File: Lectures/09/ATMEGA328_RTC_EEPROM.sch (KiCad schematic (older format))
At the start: 33 parts, among them Q1 IRLML6401, SW1 SW_SPST, U1 ATmega328P-AU, U2 24LC1025, U3 24LC1025, U4 DS1337S+, Y1 16MHz, Y2 32.768kHz

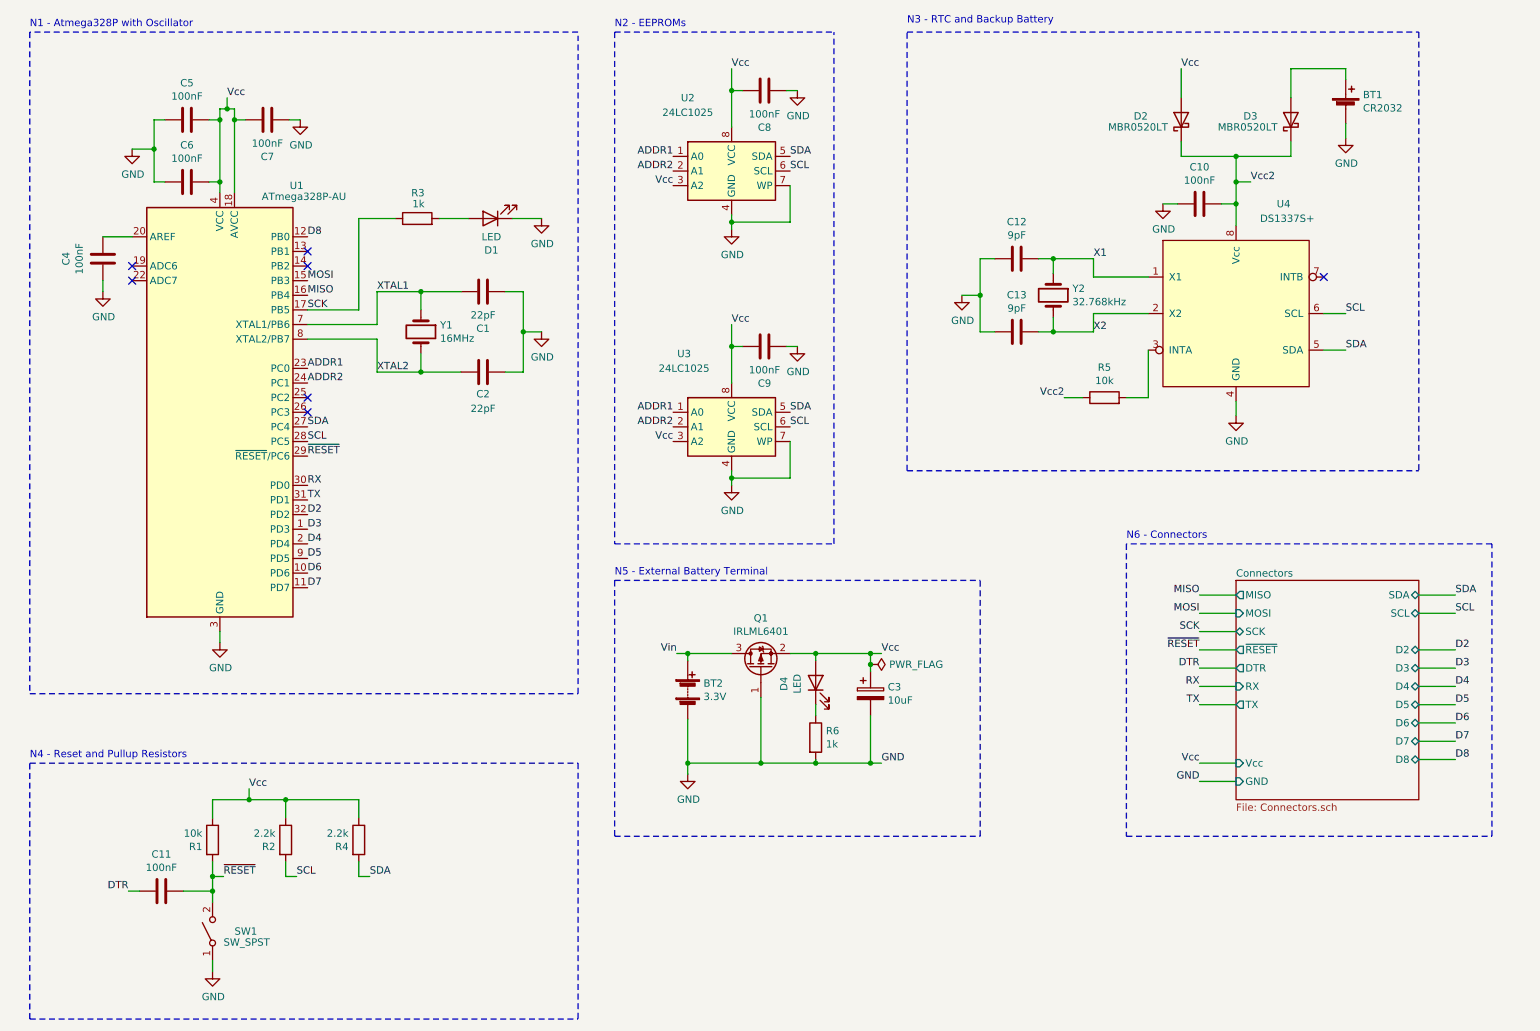
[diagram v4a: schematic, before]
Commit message: ATMEGA328 Layout
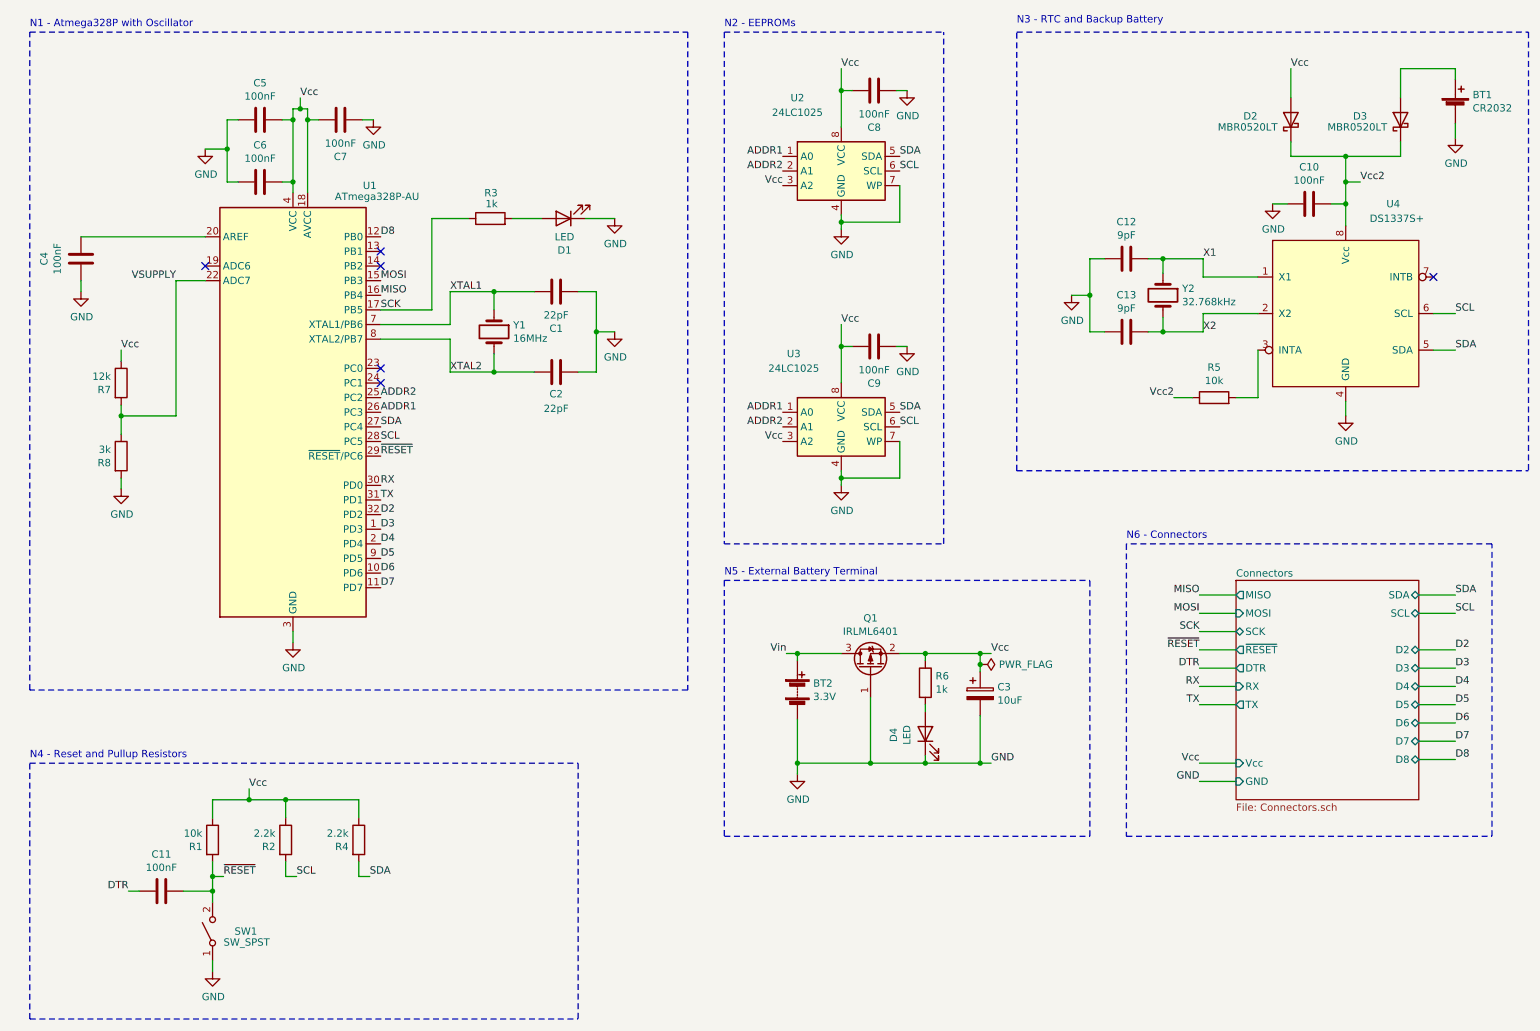
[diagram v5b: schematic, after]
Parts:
- added R7: 12k, Resistor_SMD:R_0805_2012Metric, symbol Device:R
- added R8: 3k, Resistor_SMD:R_0805_2012Metric, symbol Device:R
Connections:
- net ADDR1: now also U1.26 (PC3); no longer U1.23 (PC0)
- net ADDR2: now also U1.25 (PC2); no longer U1.24 (PC1)
- net GND: now also D4.1 (K), R8.2; no longer R6.2
- net Vcc: now also R6.1, R7.1; no longer D4.2 (A)
- net VSUPPLY: now reaches U1.22 (ADC7)
- net VSUPPLY: now also R7.2, R8.1
- new net: D4.2 (A), R6.2
- no-connect marks 7 -> 6
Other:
- moved on the sheet: BT1, BT2, C1, C10, C12, C13, C2, C3, C4, C5, C6, C7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

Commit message: Addressing and Silkscreen
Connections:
- net ADDR1: now also U1.25 (PC2); no longer U1.26 (PC3), U3.1 (A0)
- net ADDR2: now also U1.26 (PC3); no longer U1.25 (PC2), U2.2 (A1)
- net GND: now also U2.2 (A1)
- net Vcc: now also U3.1 (A0)
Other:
- moved on the sheet: C8, C9, U2, U3
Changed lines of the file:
@@
 	7500 3750 11000 3750
 Wire Notes Line
-	7000 4250 7000 750
+	7250 4250 7250 750
 Wire Notes Line
 	5500 750  5500 4250
-Wire Notes Line
-	5500 4250 7000 4250
-Text Label 6300 2750 0    50   ~ 0
+Text Label 6550 2825 0    50   ~ 0
 Vcc
 $Comp
 L Device:C C9
 U 1 1 601B0C2E
-P 6525 2900
-F 0 "C9" V 6273 2900 50  0000 C CNN
-F 1 "100nF" V 6364 2900 50  0000 C CNN
-F 2 "Capacitor_SMD:C_0603_1608Metric" H 6563 2750 50  0001 C CNN
-F 3 "~" H 6525 2900 50  0001 C CNN
-	1    6525 2900
-	0    -1   -1   0
-$EndComp
-Wire Wire Line
-	6300 3150 6300 2900
-Wire Wire Line
-	6300 2900 6375 2900
+P 6775 2900
+F 0 "C9" V 6523 2900 50  0000 C CNN
+F 1 "100nF" V 6614 2900 50  0000 C CNN
+F 2 "Capacitor_SMD:C_0603_1608Metric" H 6813 2750 50  0001 C CNN
+F 3 "~" H 6775 2900 50  0001 C CNN
+	1    6775 2900
+	0    -1   -1   0
+$EndComp
+Wire Wire Line
+	6550 3150 6550 2900
+Wire Wire Line
+	6550 2900 6625 2900
 $Comp
 L power:GND #PWR010
 U 1 1 601B0C26
-P 6750 2900
-F 0 "#PWR010" H 6750 2650 50  0001 C CNN
-F 1 "GND" H 6755 2727 50  0000 C CNN
-F 2 "" H 6750 2900 50  0001 C CNN
-F 3 "" H 6750 2900 50  0001 C CNN
-	1    6750 2900
-	1    0    0    -1
-$EndComp
-Wire Wire Line
-	6750 2900 6675 2900
-Wire Wire Line
-	6300 2900 6300 2750
-Connection ~ 6300 2900
-Text Label 6300 1000 0    50   ~ 0
+P 7000 2900
+F 0 "#PWR010" H 7000 2650 50  0001 C CNN
+F 1 "GND" H 7005 2727 50  0000 C CNN
+F 2 "" H 7000 2900 50  0001 C CNN
+F 3 "" H 7000 2900 50  0001 C CNN
+	1    7000 2900
+	1    0    0    -1
+$EndComp
+Wire Wire Line
+	7000 2900 6925 2900
+Text Label 6550 1075 0    50   ~ 0
 Vcc
 $Comp
 L Device:C C8
 U 1 1 6019A0DD
-P 6525 1150
-F 0 "C8" V 6273 1150 50  0000 C CNN
-F 1 "100nF" V 6364 1150 50  0000 C CNN
-F 2 "Capacitor_SMD:C_0603_1608Metric" H 6563 1000 50  0001 C CNN
-F 3 "~" H 6525 1150 50  0001 C CNN
-	1    6525 1150
-	0    -1   -1   0
-$EndComp
-Wire Wire Line
-	6300 1400 6300 1150
-Wire Wire Line
-	6300 1150 6375 1150
+P 6775 1150
+F 0 "C8" V 6523 1150 50  0000 C CNN
+F 1 "100nF" V 6614 1150 50  0000 C CNN
+F 2 "Capacitor_SMD:C_0603_1608Metric" H 6813 1000 50  0001 C CNN
+F 3 "~" H 6775 1150 50  0001 C CNN
+	1    6775 1150
+	0    -1   -1   0
+$EndComp
+Wire Wire Line
+	6550 1400 6550 1150
+Wire Wire Line
+	6550 1150 6625 1150
 $Comp
 L power:GND #PWR09
 U 1 1 601A1158
-P 6750 1150
-F 0 "#PWR09" H 6750 900 50  0001 C CNN
-F 1 "GND" H 6755 977 50  0000 C CNN
-F 2 "" H 6750 1150 50  0001 C CNN
-F 3 "" H 6750 1150 50  0001 C CNN
-	1    6750 1150
-	1    0    0    -1
-$EndComp
-Wire Wire Line
-	6750 1150 6675 1150
-Wire Wire Line
-	6300 1150 6300 1000
-Connection ~ 6300 1150
+P 7000 1150
+F 0 "#PWR09" H 7000 900 50  0001 C CNN
+F 1 "GND" H 7005 977 50  0000 C CNN
+F 2 "" H 7000 1150 50  0001 C CNN
+F 3 "" H 7000 1150 50  0001 C CNN
+	1    7000 1150
+	1    0    0    -1
+$EndComp
+Wire Wire Line
+	7000 1150 6925 1150
 $Comp
 L power:GND #PWR08
 U 1 1 600E01FF
-P 6300 3850
-F 0 "#PWR08" H 6300 3600 50  0001 C CNN
-F 1 "GND" H 6305 3677 50  0000 C CNN
-F 2 "" H 6300 3850 50  0001 C CNN
-F 3 "" H 6300 3850 50  0001 C CNN
-	1    6300 3850
-	1    0    0    -1
-$EndComp
-$Comp
-L power:GND #PWR07
-U 1 1 600DFD7C
-P 6300 2100
-F 0 "#PWR07" H 6300 1850 50  0001 C CNN
-F 1 "GND" H 6305 1927 50  0000 C CNN
-F 2 "" H 6300 2100 50  0001 C CNN
-F 3 "" H 6300 2100 50  0001 C CNN
-	1    6300 2100
+P 6550 3925
+F 0 "#PWR08" H 6550 3675 50  0001 C CNN
+F 1 "GND" H 6555 3752 50  0000 C CNN
+F 2 "" H 6550 3925 50  0001 C CNN
+F 3 "" H 6550 3925 50  0001 C CNN
+	1    6550 3925
 	1    0    0    -1
 $EndComp
 Text Notes 5500 725  0    50   ~ 0
 N2 - EEPROMs
-Wire Notes Line
-	5500 750  7000 750
-Wire Wire Line
-	6300 2050 6300 2000
-Connection ~ 6300 2050
-Wire Wire Line
-	6700 2050 6300 2050
-Wire Wire Line
-	6700 1800 6700 2050
-Wire Wire Line
-	6300 3800 6300 3750
-Connection ~ 6300 3800
-Wire Wire Line
-	6700 3800 6300 3800
-Wire Wire Line
-	6700 3550 6700 3800
-Wire Wire Line
-	6300 3850 6300 3800
-Text Label 5900 3450 2    50   ~ 0
-ADDR2
-Text Label 5900 1700 2    50   ~ 0
-ADDR2
-Text Label 5900 1600 2    50   ~ 0
-ADDR1
-Text Label 5900 3350 2    50   ~ 0
-ADDR1
-Text Label 6700 3350 0    50   ~ 0
+Text Label 6950 3350 0    50   ~ 0
 SDA
-Text Label 6700 1600 0    50   ~ 0
+Text Label 6950 1600 0    50   ~ 0
 SDA
-Text Label 6700 3450 0    50   ~ 0
+Text Label 6950 3450 0    50   ~ 0
 SCL
-Text Label 6700 1700 0    50   ~ 0
+Text Label 6950 1700 0    50   ~ 0
 SCL
-Text Label 5900 3550 2    50   ~ 0
-Vcc
-Text Label 5900 1800 2    50   ~ 0
-Vcc
-Wire Wire Line
-	6300 2100 6300 2050
-$Comp
-L Memory_EEPROM:24LC1025 U2
-U 1 1 60098B6E
-P 6300 1700
-F 0 "U2" H 6000 2200 50  0000 C CNN
-F 1 "24LC1025" H 6000 2100 50  0000 C CNN
-F 2 "Package_SO:SOIJ-8_5.3x5.3mm_P1.27mm" H 6300 1700 50  0001 C CNN
-F 3 "http://ww1.microchip.com/downloads/en/DeviceDoc/21941B.pdf" H 6300 1700 50  0001 C CNN
-	1    6300 1700
-	1    0    0    -1
-$EndComp
+Text Label 6150 3550 2    50   ~ 0
+Vcc
+Text Label 6150 1800 2    50   ~ 0
+Vcc
 $Comp
 L Memory_EEPROM:24LC1025 U3
 U 1 1 600AAAA0
-P 6300 3450
-F 0 "U3" H 5975 3950 50  0000 C CNN
-F 1 "24LC1025" H 5975 3850 50  0000 C CNN
-F 2 "Package_SO:SOIJ-8_5.3x5.3mm_P1.27mm" H 6300 3450 50  0001 C CNN
-F 3 "http://ww1.microchip.com/downloads/en/DeviceDoc/21941B.pdf" H 6300 3450 50  0001 C CNN
-	1    6300 3450
+P 6550 3450
+F 0 "U3" H 6225 3950 50  0000 C CNN
+F 1 "24LC1025" H 6225 3850 50  0000 C CNN
+F 2 "Package_SO:SOIJ-8_5.3x5.3mm_P1.27mm" H 6550 3450 50  0001 C CNN
+F 3 "http://ww1.microchip.com/downloads/en/DeviceDoc/21941B.pdf" H 6550 3450 50  0001 C CNN
+	1    6550 3450
 	1    0    0    -1
 $EndComp
@@
 	-1   0    0    1
 $EndComp
+Text Label 3150 3250 0    50   ~ 0
+ADDR1
 Text Label 3150 3350 0    50   ~ 0
-ADDR1
-Text Label 3150 3250 0    50   ~ 0
 ADDR2
 Text Label 3150 3550 0    50   ~ 0
@@
 Wire Wire Line
 	6875 5750 7250 5750
+Wire Notes Line
+	5500 750  7250 750
+Wire Notes Line
+	5500 4250 7250 4250
+Text Label 6150 3450 2    50   ~ 0
+ADDR2
+Text Label 6150 1600 2    50   ~ 0
+ADDR1
+Text Label 6150 3350 2    50   ~ 0
+Vcc
+Wire Wire Line
+	6550 3750 6550 3875
+Wire Wire Line
+	6950 3875 6550 3875
+Wire Wire Line
+	6950 3550 6950 3875
+Connection ~ 6550 3875
+Wire Wire Line
+	6550 3875 6550 3925
+$Comp
+L power:GND #PWR07
+U 1 1 600DFD7C
+P 6550 2175
+F 0 "#PWR07" H 6550 1925 50  0001 C CNN
+F 1 "GND" H 6555 2002 50  0000 C CNN
+F 2 "" H 6550 2175 50  0001 C CNN
+F 3 "" H 6550 2175 50  0001 C CNN
+	1    6550 2175
+	1    0    0    -1
+$EndComp
+Wire Wire Line
+	6950 2125 6550 2125
+Wire Wire Line
+	6950 1800 6950 2125
+Connection ~ 6550 2125
+Wire Wire Line
+	6550 2125 6550 2175
+Wire Wire Line
+	6550 2000 6550 2050
+$Comp
+L Memory_EEPROM:24LC1025 U2
+U 1 1 60098B6E
+P 6550 1700
+F 0 "U2" H 6250 2200 50  0000 C CNN
+F 1 "24LC1025" H 6250 2100 50  0000 C CNN
+F 2 "Package_SO:SOIJ-8_5.3x5.3mm_P1.27mm" H 6550 1700 50  0001 C CNN
+F 3 "http://ww1.microchip.com/downloads/en/DeviceDoc/21941B.pdf" H 6550 1700 50  0001 C CNN
+	1    6550 1700
+	1    0    0    -1
+$EndComp
+Wire Wire Line
+	6150 1700 5875 1700
+Wire Wire Line
+	5875 1700 5875 2050
+Wire Wire Line
+	5875 2050 6550 2050
+Connection ~ 6550 2050
+Wire Wire Line
+	6550 2050 6550 2125
+Wire Wire Line
+	6550 2900 6550 2825
+Connection ~ 6550 2900
+Wire Wire Line
+	6550 1150 6550 1075
+Connection ~ 6550 1150
 $EndSCHEMATC

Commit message: EEPROM addresses set by jumpers
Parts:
- added JP1, JP2, JP3, JP4: SJ, Jumper:SolderJumper-3_P1.3mm_Open_Pad1.0x1.5mm, symbol Jumper:SolderJumper_3_Open
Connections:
- net GND: now also JP1.1 (A), JP2.1 (A), JP3.1 (A), JP4.1 (A); no longer U2.2 (A1)
- net Vcc: now also JP1.3 (B), JP2.3 (B), JP3.3 (B), JP4.3 (B); no longer U3.1 (A0)
- net ADDR1: no longer names the net of U2.1 (A0)
- net ADDR1: now also JP1.2 (C); no longer U1.25 (PC2)
- net ADDR2: no longer names the net of U1.26 (PC3)
- net ADDR2: no longer U3.2 (A1)
- new net: JP2.2 (C), U2.2 (A1)
- new net: JP3.2 (C), U3.1 (A0)
- new net: JP4.2 (C), U3.2 (A1)
- no-connect marks 6 -> 8
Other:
- moved on the sheet: C8, C9, U2, U3
